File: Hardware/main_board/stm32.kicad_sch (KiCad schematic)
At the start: 36 parts, among them U7 STM32WB55RGVx, Y1 32MHz, Y2 32.768K

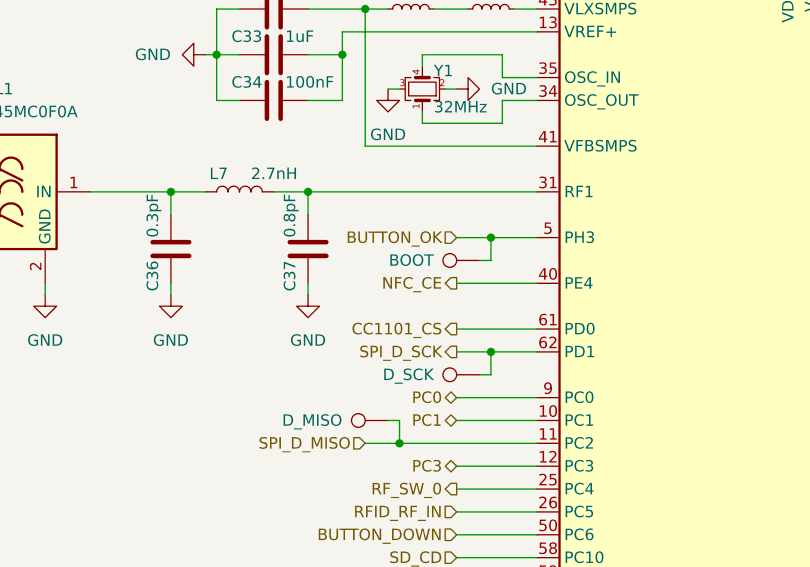
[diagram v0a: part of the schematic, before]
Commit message: sch: rename NFC_CE to NFC_CS
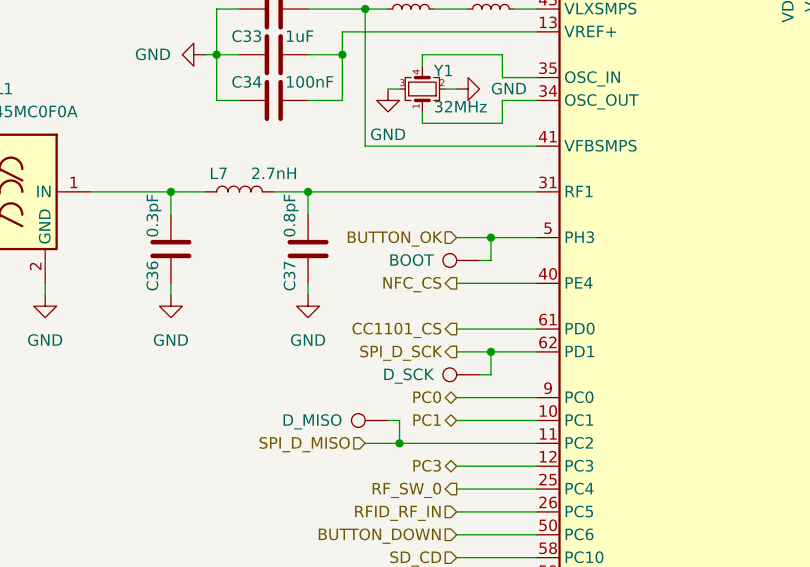
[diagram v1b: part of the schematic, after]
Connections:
- net NFC_CE renamed NFC_CS
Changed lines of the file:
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@@
 		(shape input)
 		(at 187.96 135.89 0)
-		(effects
-			(font
-				(size 1.27 1.27)
-			)
-			(justify left)
-		)
-	)
-	(hierarchical_label "NFC_CE"
+		(fields_autoplaced yes)
+		(effects
+			(font
+				(size 1.27 1.27)
+			)
+			(justify left)
+		)
+	)
+	(hierarchical_label "NFC_CS"
 		(shape output)
 		(at 127 102.87 180)
@@
 		(shape bidirectional)
 		(at 187.96 85.09 0)
+		(fields_autoplaced yes)
 		(effects
 			(font
@@
 		(shape bidirectional)
 		(at 187.96 82.55 0)
+		(fields_autoplaced yes)
 		(effects
 			(font
@@
 		(shape output)
 		(at 187.96 148.59 0)
+		(fields_autoplaced yes)
 		(effects
 			(font
@@
 		(shape bidirectional)
 		(at 127 123.19 180)
+		(fields_autoplaced yes)
 		(effects
 			(font
@@
 		(shape output)
 		(at 187.96 113.03 0)
+		(fields_autoplaced yes)
 		(effects
 			(font
@@
 		(shape bidirectional)
 		(at 127 118.11 180)
+		(fields_autoplaced yes)
 		(effects
 			(font
@@
 		(shape bidirectional)
 		(at 127 115.57 180)
+		(fields_autoplaced yes)
 		(effects
 			(font
@@
 		(shape output)
 		(at 187.96 74.93 0)
+		(fields_autoplaced yes)
 		(effects
 			(font
@@
 		(shape input)
 		(at 187.96 67.31 0)
+		(fields_autoplaced yes)
 		(effects
 			(font
@@
 		(shape input)
 		(at 187.96 105.41 0)
+		(fields_autoplaced yes)
 		(effects
 			(font
@@
 		(shape output)
 		(at 187.96 110.49 0)
+		(fields_autoplaced yes)
 		(effects
 			(font
@@
 		(shape bidirectional)
 		(at 187.96 92.71 0)
+		(fields_autoplaced yes)
 		(effects
 			(font
@@
 		(shape output)
 		(at 187.96 125.73 0)
+		(fields_autoplaced yes)
 		(effects
 			(font
@@
 		(shape bidirectional)
 		(at 187.96 100.33 0)
+		(fields_autoplaced yes)
 		(effects
 			(font
@@
 		(shape bidirectional)
 		(at 187.96 118.11 0)
+		(fields_autoplaced yes)
 		(effects
 			(font
@@
 		(shape bidirectional)
 		(at 187.96 69.85 0)
+		(fields_autoplaced yes)
 		(effects
 			(font
@@
 		(shape input)
 		(at 187.96 138.43 0)
+		(fields_autoplaced yes)
 		(effects
 			(font
@@
 		(shape input)
 		(at 187.96 128.27 0)
+		(fields_autoplaced yes)
 		(effects
 			(font
@@
 		(shape output)
 		(at 198.12 80.01 0)
+		(fields_autoplaced yes)
 		(effects
 			(font
@@
 		(shape bidirectional)
 		(at 187.96 146.05 0)
+		(fields_autoplaced yes)
 		(effects
 			(font
@@
 		(shape output)
 		(at 187.96 143.51 0)
+		(fields_autoplaced yes)
 		(effects
 			(font
@@
 		(shape output)
 		(at 203.2 123.19 0)
+		(fields_autoplaced yes)
 		(effects
 			(font
@@
 		(shape output)
 		(at 187.96 130.81 0)
+		(fields_autoplaced yes)
 		(effects
 			(font
@@
 		(shape input)
 		(at 187.96 102.87 0)
+		(fields_autoplaced yes)
 		(effects
 			(font
@@
 		(shape input)
 		(at 187.96 140.97 0)
+		(fields_autoplaced yes)
 		(effects
 			(font
@@
 		(shape input)
 		(at 203.2 120.65 0)
+		(fields_autoplaced yes)
 		(effects
 			(font
@@
 		(shape output)
 		(at 187.96 87.63 0)
+		(fields_autoplaced yes)
 		(effects
 			(font
@@
 		(shape output)
 		(at 187.96 133.35 0)
+		(fields_autoplaced yes)
 		(effects
 			(font
@@
 		(shape bidirectional)
 		(at 187.96 77.47 0)
+		(fields_autoplaced yes)
 		(effects
 			(font
@@
 		(shape bidirectional)
 		(at 187.96 115.57 0)
+		(fields_autoplaced yes)
 		(effects
 			(font
@@
 		(shape output)
 		(at 187.96 90.17 0)
+		(fields_autoplaced yes)
 		(effects
 			(font
@@
 		(shape output)
 		(at 187.96 72.39 0)
-		(effects
-			(font
+		(fields_autoplaced yes)
+		(effects
+			(font

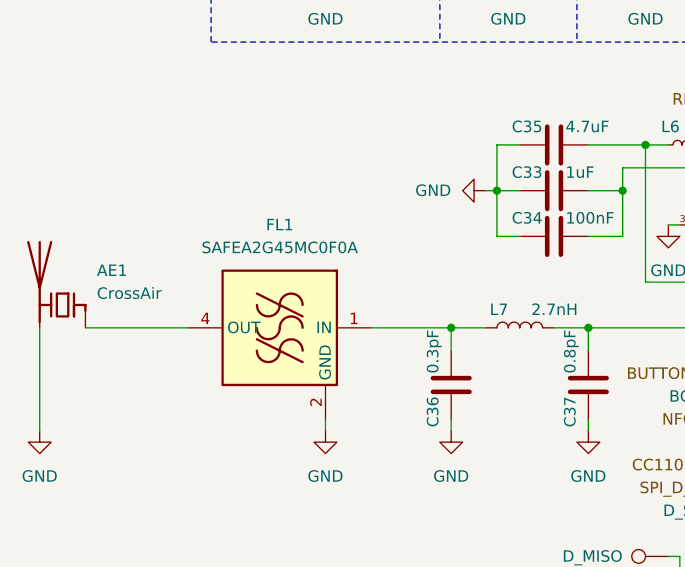
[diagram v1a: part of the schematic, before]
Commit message: sch: replace the SAW filter with a multilayer one
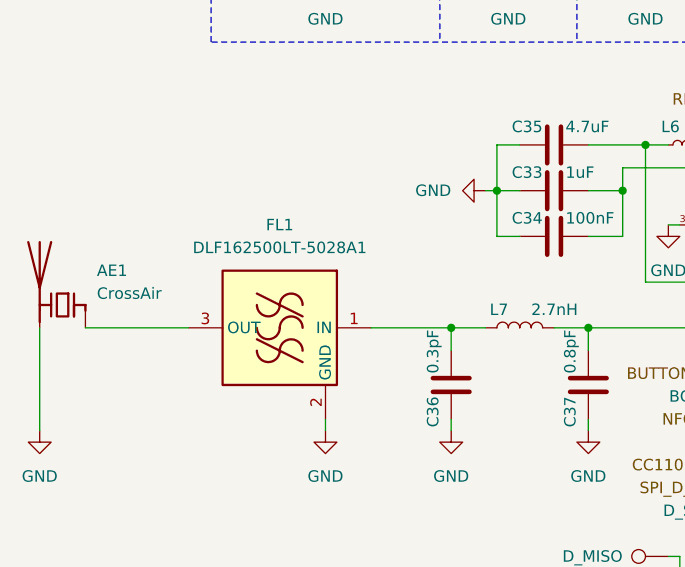
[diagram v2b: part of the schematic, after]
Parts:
- removed FL1: SAFEA2G45MC0F0A, Filter:Filter_1411-5_1.4x1.1mm, symbol Library:SAFEA2G45MC0F0A
- added FL1: DLF162500LT-5028A1, symbol Library:DLF162500LT-5028A1
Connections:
- net GND: now also FL1.2 (GND), FL1.4 (GND)
- net at C36.2, L7.1: now also FL1.1 (IN)
- net at AE1.1 (FEED): now also FL1.3 (OUT)
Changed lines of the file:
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@@
-	)
-	(symbol
-		(lib_id "Library:SAFEA2G45MC0F0A")
-		(at 76.2 92.71 0)
-		(mirror y)
-		(unit 1)
-		(exclude_from_sim no)
-		(in_bom yes)
-		(on_board yes)
-		(dnp no)
-		(fields_autoplaced yes)
-		(property "Reference" "FL1"
-			(at 76.2 81.28 0)
-			(effects
-				(font
-					(size 1.27 1.27)
-				)
-			)
-		)
-		(property "Value" "SAFEA2G45MC0F0A"
-			(at 76.2 83.82 0)
-			(effects
-				(font
-					(size 1.27 1.27)
-				)
-			)
-		)
-		(property "Footprint" "Filter:Filter_1411-5_1.4x1.1mm"
-			(at 76.2 92.71 0)
-			(effects
-				(font
-					(size 1.27 1.27)
-				)
-				(hide yes)
-			)
-		)
-		(property "Datasheet" ""
-			(at 76.2 92.71 0)
-			(effects
-				(font
-					(size 1.27 1.27)
-				)
-				(hide yes)
-			)
-		)
-		(property "Description" ""
-			(at 76.2 92.71 0)
-			(effects
-				(font
-					(size 1.27 1.27)
-				)
-				(hide yes)
-			)
-		)
-		(pin "1"
-		)
-		(pin "2"
-		)
-		(pin "5"
-		)
-		(pin "4"
-		)
-		(pin "6"
-		)
-		(pin "3"
-		)
-		(instances
-			(project ""
-				(path "/16216a68-6dea-41d7-8e15-2cc84f72f8e2/8225a072-bd5c-4ab0-988a-5acfd87a3b3a"
-					(reference "FL1")
-					(unit 1)
-				)
-			)
-		)
 	)
 	(symbol
@@
 					(unit 1)
 				)
+			)
+		)
+	)
+	(symbol
+		(lib_id "Library:DLF162500LT-5028A1")
+		(at 76.2 92.71 0)
+		(mirror y)
+		(unit 1)
+		(exclude_from_sim no)
+		(in_bom yes)
+		(on_board yes)
+		(dnp no)
+		(fields_autoplaced yes)
+		(property "Reference" "FL1"
+			(at 76.2 81.28 0)
+			(effects
+				(font
+					(size 1.27 1.27)
+				)
+			)
+		)
+		(property "Value" "DLF162500LT-5028A1"
+			(at 76.2 83.82 0)
+			(effects
+				(font
+					(size 1.27 1.27)
+				)
+			)
+		)
+		(property "Footprint" ""
+			(at 76.2 85.09 0)
+			(effects
+				(font
+					(size 1.27 1.27)
+				)
+				(hide yes)
+			)
+		)
+		(property "Datasheet" ""
+			(at 76.2 85.09 0)
+			(effects
+				(font
+					(size 1.27 1.27)
+				)
+				(hide yes)
+			)
+		)
+		(property "Description" ""
+			(at 76.2 85.09 0)
+			(effects
+				(font
+					(size 1.27 1.27)
+				)
+				(hide yes)
+			)
+		)
+		(pin "1"
+		)
+		(pin "2"
+		)
+		(pin "4"
+		)
+		(pin "3"
+		)
+		(instances
+			(project ""
+				(path "/16216a68-6dea-41d7-8e15-2cc84f72f8e2/8225a072-bd5c-4ab0-988a-5acfd87a3b3a"
+					(reference "FL1")
+					(unit 1)
+				)

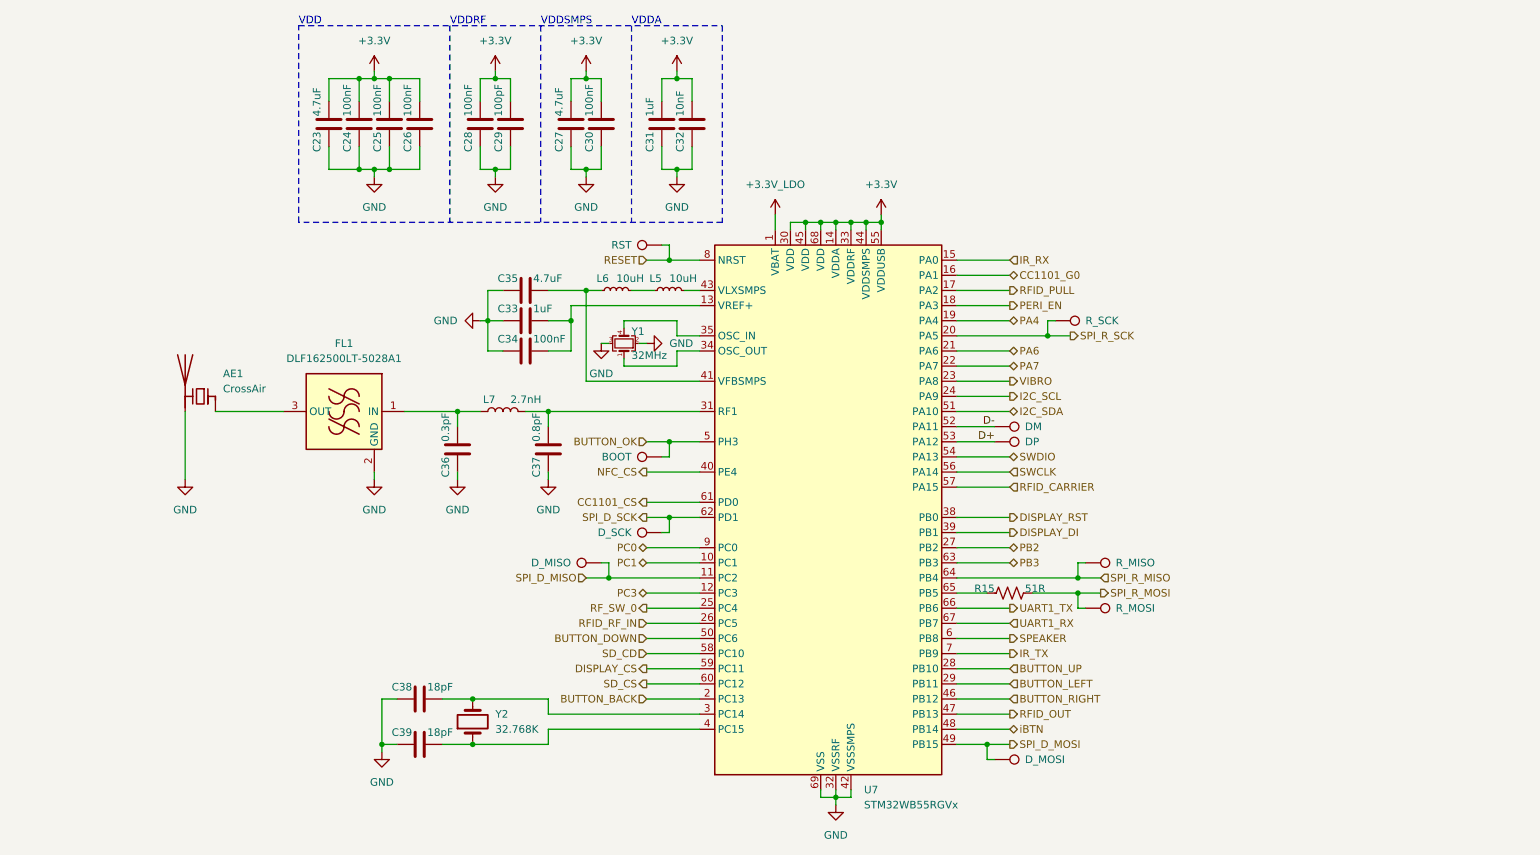
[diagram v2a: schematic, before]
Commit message: sch: add some part of footprints
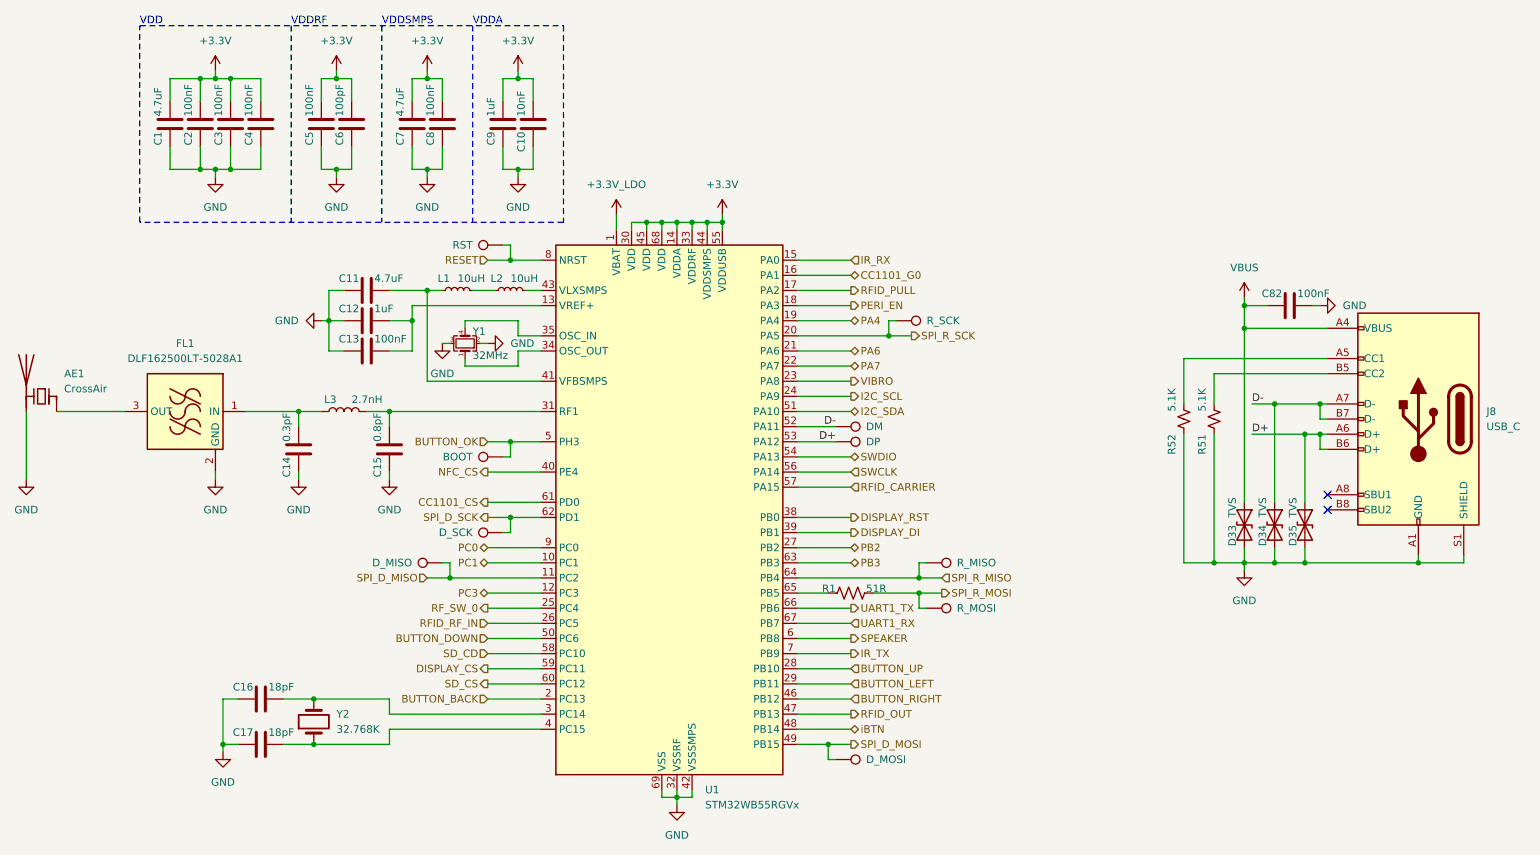
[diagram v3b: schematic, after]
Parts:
- added C82: 100nF, Capacitor_SMD:C_0402_1005Metric, symbol Device:C
- added D33, D34, D35: TVS, Diode_SMD:D_0201_0603Metric, symbol Device:D_TVS
- added J8: USB_C, symbol Connector:USB_C_Receptacle_USB2.0_16P
- added R51, R52: 5.1K, Resistor_SMD:R_0402_1005Metric, symbol Device:R_Small_US
- C1: renamed from C23; footprint (none) -> Capacitor_SMD:C_0402_1005Metric
- C10: renamed from C32; footprint (none) -> Capacitor_SMD:C_0402_1005Metric
- C11: renamed from C35; footprint (none) -> Capacitor_SMD:C_0402_1005Metric
- C12: renamed from C33; footprint (none) -> Capacitor_SMD:C_0402_1005Metric
- C13: renamed from C34; footprint (none) -> Capacitor_SMD:C_0402_1005Metric
- C14: renamed from C36; footprint (none) -> Capacitor_SMD:C_0402_1005Metric
- C15: renamed from C37; footprint (none) -> Capacitor_SMD:C_0402_1005Metric
- C16: renamed from C38; footprint (none) -> Capacitor_SMD:C_0402_1005Metric
- C17: renamed from C39; footprint (none) -> Capacitor_SMD:C_0402_1005Metric
- C2: renamed from C24; footprint (none) -> Capacitor_SMD:C_0402_1005Metric
- C3: renamed from C25; footprint (none) -> Capacitor_SMD:C_0402_1005Metric
- C4: renamed from C26; footprint (none) -> Capacitor_SMD:C_0402_1005Metric
- C5: renamed from C28; footprint (none) -> Capacitor_SMD:C_0402_1005Metric
- C6: renamed from C29; footprint (none) -> Capacitor_SMD:C_0402_1005Metric
- C7: renamed from C27; footprint (none) -> Capacitor_SMD:C_0402_1005Metric
- C8: renamed from C30; footprint (none) -> Capacitor_SMD:C_0402_1005Metric
- C9: renamed from C31; footprint (none) -> Capacitor_SMD:C_0402_1005Metric
- L1: renamed from L6; footprint (none) -> Inductor_SMD:L_0805_2012Metric
- L2: renamed from L5; footprint (none) -> Inductor_SMD:L_0805_2012Metric
- L3: renamed from L7; footprint (none) -> Inductor_SMD:L_0402_1005Metric
- R1: renamed from R15; footprint (none) -> Resistor_SMD:R_0402_1005Metric
- TP1: renamed from TP21; footprint (none) -> TestPoint:TestPoint_Pad_D1.0mm
- TP10: renamed from TP31; footprint (none) -> TestPoint:TestPoint_Pad_D1.0mm
- TP2: renamed from TP26; footprint (none) -> TestPoint:TestPoint_Pad_D1.0mm
- TP3: renamed from TP27; footprint (none) -> TestPoint:TestPoint_Pad_D1.0mm
- TP4: renamed from TP28; footprint (none) -> TestPoint:TestPoint_Pad_D1.0mm
- TP5: renamed from TP23; footprint (none) -> TestPoint:TestPoint_Pad_D1.0mm
- TP6: renamed from TP24; footprint (none) -> TestPoint:TestPoint_Pad_D1.0mm
- TP7: renamed from TP25; footprint (none) -> TestPoint:TestPoint_Pad_D1.0mm
- TP8: renamed from TP29; footprint (none) -> TestPoint:TestPoint_Pad_D1.0mm
- TP9: renamed from TP30; footprint (none) -> TestPoint:TestPoint_Pad_D1.0mm
- Y1: footprint (none) -> Crystal:Crystal_SMD_2520-4Pin_2.5x2.0mm
- Y2: footprint (none) -> Crystal:Crystal_SMD_2012-2Pin_2.0x1.2mm
- renumbered U7 to U1
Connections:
- net D+: now also D35.1 (A1), J8.A6 (D+), J8.B6 (D+)
- net D-: now also D34.1 (A1), J8.A7 (D-), J8.B7 (D-)
- net GND: now also C82.2, D33.2 (A2), D34.2 (A2), D35.2 (A2), J8.A1 (GND), J8.A12 (GND), J8.B1 (GND), J8.B12 (GND), J8.S1 (SHIELD), R51.1, R52.1
- new net: J8.A5 (CC1), R52.2
- new net: J8.B5 (CC2), R51.2
- new net VBUS: C82.1, D33.1 (A1), J8.A4 (VBUS), J8.A9 (VBUS), J8.B4 (VBUS), J8.B9 (VBUS)
- no-connect marks 0 -> 2
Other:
- moved on the sheet: AE1, C1, C10, C11, C12, C13, C14, C15, C16, C17, C2, C3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
